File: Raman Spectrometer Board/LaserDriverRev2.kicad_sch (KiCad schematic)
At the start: 40 parts, among them Q5 2N7002, Q6 IRF9Z34, SW1 SW_DPDT_x2, U3 LT1009, U4 OPA4192

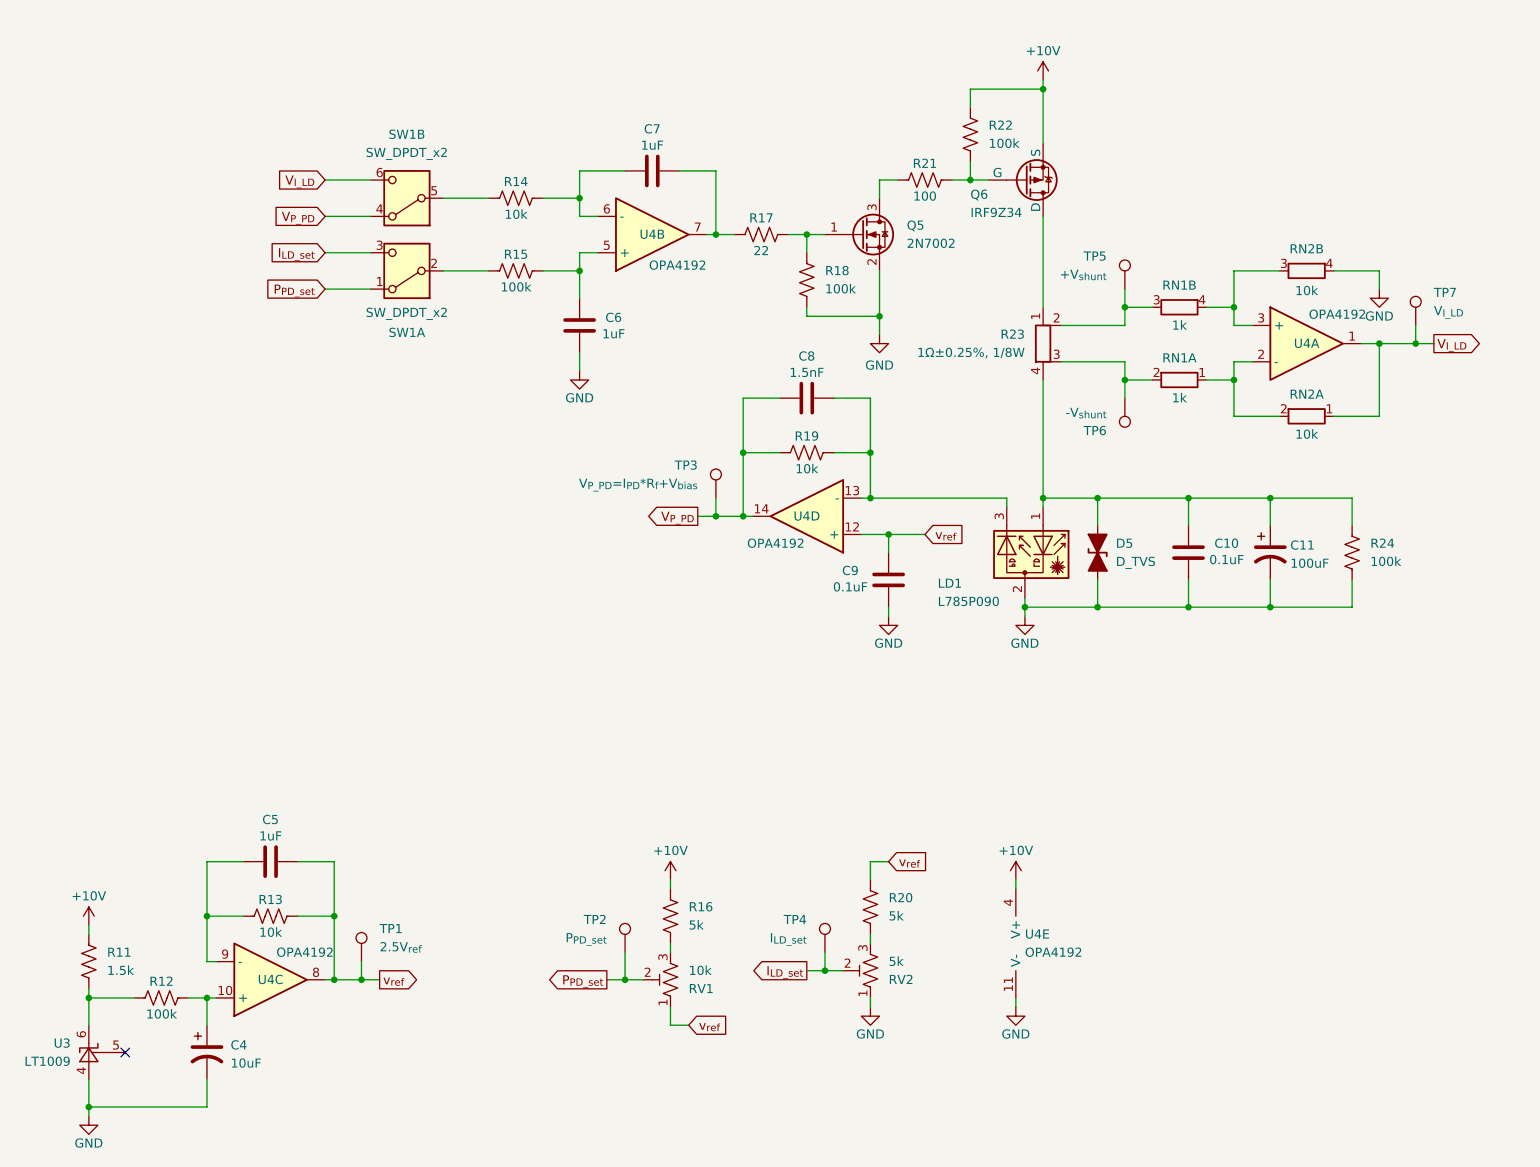
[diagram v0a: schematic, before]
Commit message: Added some laser driver footprints and 3d models
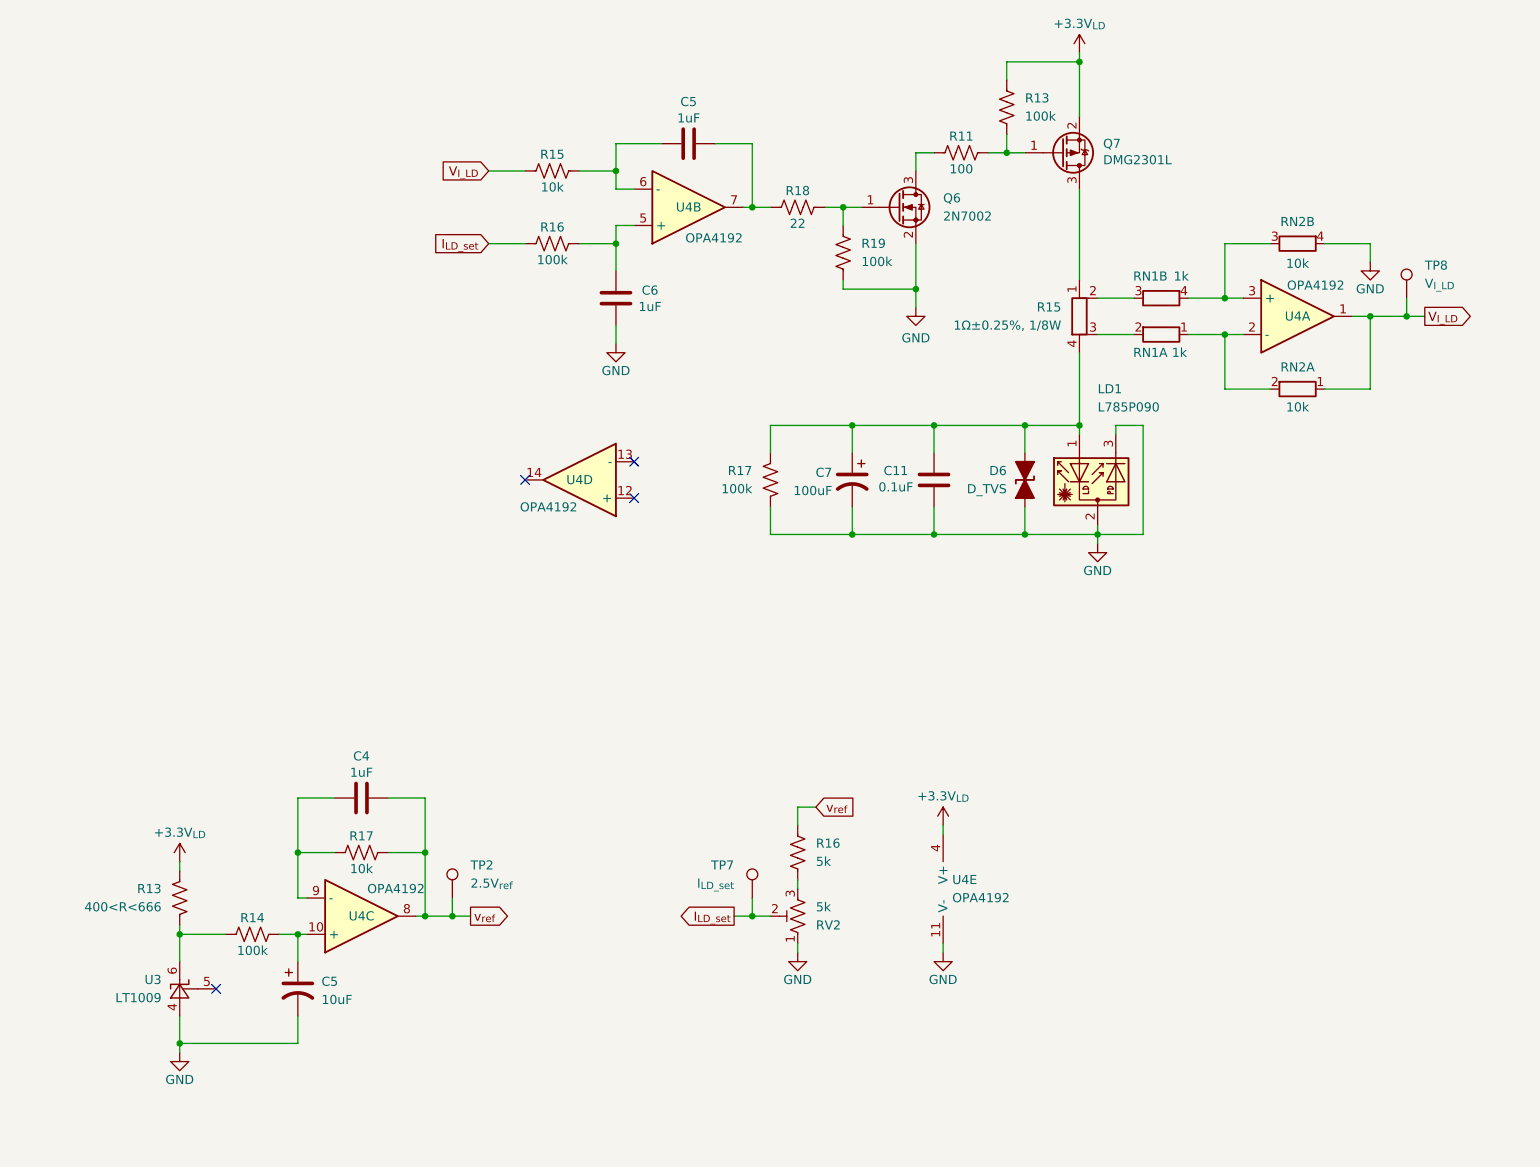
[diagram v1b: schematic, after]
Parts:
- removed C11: 100uF, Capacitor_SMD:CP_Elec_6.3x5.8, symbol Device:C_Polarized_US
- removed C4: 10uF, Capacitor_SMD:CP_Elec_5x5.8, symbol Device:C_Polarized_US
- removed C7: 1uF, Capacitor_SMD:C_0603_1608Metric, symbol Device:C
- removed C8: 1.5nF, Capacitor_SMD:C_0603_1608Metric, symbol Device:C
- removed C9: 0.1uF, Capacitor_SMD:C_0603_1608Metric, symbol Device:C
- removed D5: D_TVS, Diode_SMD:D_0603_1608Metric, symbol Device:D_TVS_Filled
- removed Q5: 2N7002, Package_TO_SOT_SMD:SOT-23, symbol Transistor_FET:2N7002
- removed Q6: IRF9Z34, Package_TO_SOT_THT:TO-220-3_Horizontal_TabUp, symbol Simulation_SPICE:PMOS
- removed R11: 1.5k, Resistor_SMD:R_0603_1608Metric, symbol Device:R_US
- removed R12, R24: 100k, Resistor_SMD:R_0603_1608Metric, symbol Device:R_US
- removed R16, R20: 5k, Resistor_SMD:R_0603_1608Metric, symbol Device:R_US
- removed R17: 22, Resistor_SMD:R_0603_1608Metric, symbol Device:R_US
- removed R23: 1Ω±0.25%, 1/8W, LD_Library:R_Shunt_0805_2012Metric, symbol Device:R_Shunt
- removed RV1: 10k, Potentiometer_THT:Potentiometer_Bourns_3296W_Vertical, symbol Device:R_Potentiometer_Trim_US
- removed SW1: SW_DPDT_x2, Button_Switch_SMD:SW_DPDT_CK_JS202011JCQN, symbol Switch:SW_DPDT_x2
- removed TP2: P_{PD_set}, TestPoint:TestPoint_Pad_D1.5mm, symbol Connector:TestPoint
- removed TP3: V_{P_PD}=I_{PD}*R_{f}+V_{bias}, TestPoint:TestPoint_Pad_D1.5mm, symbol Connector:TestPoint
- removed TP5: +V_{shunt}, TestPoint:TestPoint_Pad_D1.5mm, symbol Connector:TestPoint
- removed TP6: -V_{shunt}, TestPoint:TestPoint_Pad_D1.5mm, symbol Connector:TestPoint
- added C4: 1uF, Capacitor_SMD:C_0603_1608Metric, symbol Device:C
- added C5: 10uF, Capacitor_SMD:CP_Elec_5x5.8, symbol Device:C_Polarized_US
- added C7: 100uF, Capacitor_SMD:CP_Elec_6.3x5.8, symbol Device:C_Polarized_US
- added D6: D_TVS, Diode_SMD:D_0603_1608Metric, symbol Device:D_TVS_Filled
- added Q6: 2N7002, Package_TO_SOT_SMD:SOT-23, symbol Transistor_FET:2N7002
- added Q7: DMG2301L, Package_TO_SOT_SMD:SOT-23, symbol Transistor_FET:DMG2301L
- added R15: 1Ω±0.25%, 1/8W, LD_Library:R_Shunt_0805_2012Metric, symbol Device:R_Shunt
- added R16, R17: 100k, Resistor_SMD:R_0603_1608Metric, symbol Device:R_US
- added R16: 5k, Resistor_SMD:R_0603_1608Metric, symbol Device:R_US
- added R17: 10k, Resistor_SMD:R_0603_1608Metric, symbol Device:R_US
- R13: value 10k -> 400<R<666
- R14: value 10k -> 100k
- R15: value 100k -> 10k
- R18: value 100k -> 22
- R19: value 10k -> 100k; Price $0.23000 -> (none)
- renumbered C10 to C11, R21 to R11, R22 to R13, TP1 to TP2, TP4 to TP7, TP7 to TP8
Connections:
- net GND: now also LD1.3, R19.2, C5.2, C7.2, D6.1 (A1), Q6.2 (S), R17.2; no longer R18.2
- net I_{LD_set}: now also R16.1
- net V_{I_LD}: now also R15.1
- net v_{ref}: now also C4.2, R16.1, R17.2; no longer C5.2, R13.2, U4.12 (+)
- net at U4.10 (+): now also R14.2, C5.1
- net at R11.2, R13.2: now also Q7.1 (G)
- net at R18.1: now also C5.2, U4.7
- net at RN1.2 (R1.2): now also R15.3
- net at C6.2, U4.5 (+): now also R16.2; no longer R15.2
- net at U4.6 (-): now also C5.1, R15.2; no longer R14.2
- net at RV2.3: now also R16.2
- net at RN1.3 (R2.1): now also R15.2
- net at C11.1, LD1.1: now also C7.1, D6.2 (A2), R15.4, R17.1
- net at U3.6 (K), U3.8 (K): now also R13.2, R14.1
- net at R11.1: now also Q6.3 (D)
- net +10V renamed +3.3V_{LD}
- net +3.3V_{LD}: now also R13.1, Q7.2 (S)
- net V_{P_PD}: no longer names the net of R19.1
- net V_{P_PD}: now also R18.2, Q6.1 (G); no longer U4.14
- new net: C4.1, R17.1, U4.9 (-)
- new net: Q7.3 (D), R15.1
- now unconnected: U4.13 (-)
- no-connect marks 1 -> 4
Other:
- moved on the sheet: C11, LD1, R11, R13, RN1A, RN1B, RN2A, RN2B, RV2, TP2, TP7, TP8

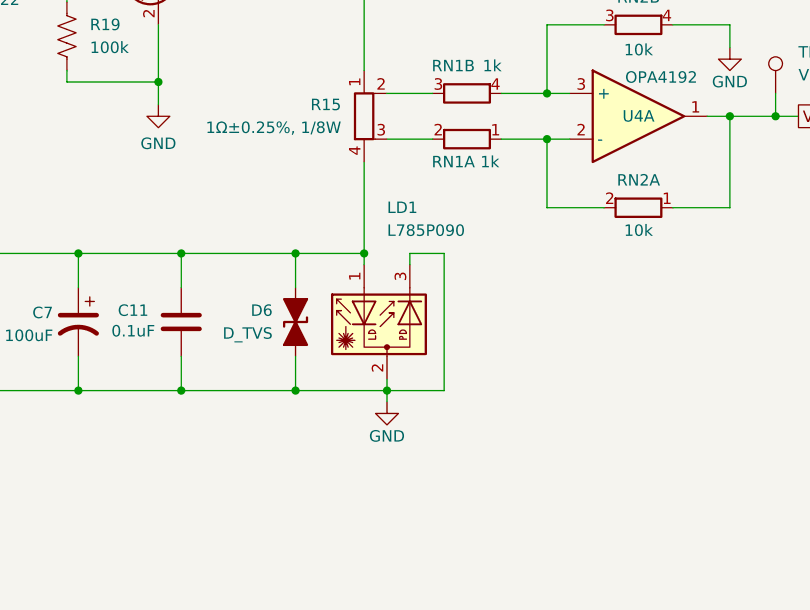
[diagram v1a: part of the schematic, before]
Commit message: Validated all footprints and models
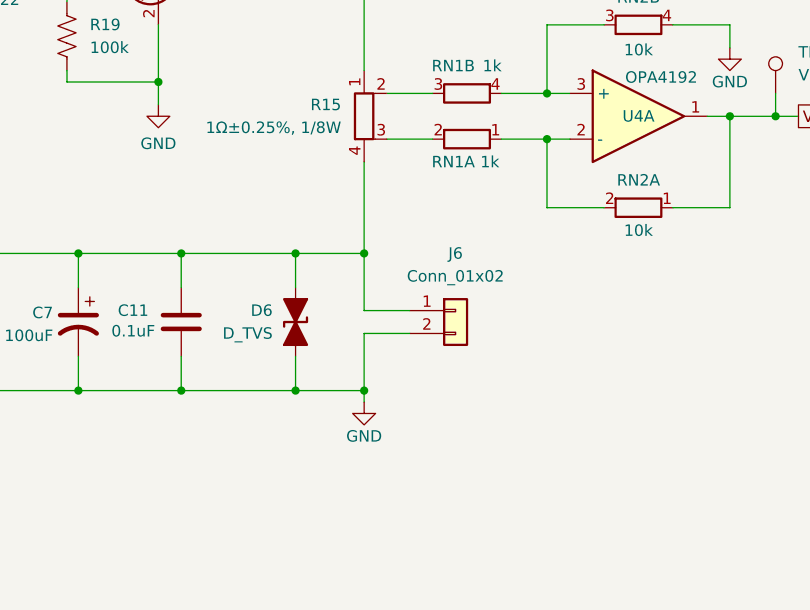
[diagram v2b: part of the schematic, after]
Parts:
- removed LD1: L785P090, LD_Library:S7060R - Laser Diode Socket for Ø5.6 mm Laser, 3 Pin, symbol Device:D_Laser_Photo_PType
- added J6: Conn_01x02, Connector_JST:JST_EH_S2B-EH_1x02_P2.50mm_Horizontal, symbol Connector_Generic:Conn_01x02
- R15: footprint LD_Library:R_Shunt_0805_2012Metric -> LaserDriverRev2Library:R_Shunt_0805_2012Metric
- RN1, RN2: footprint Resistor_SMD:R_Array_Convex_2x0606 -> LaserDriverRev2Library:R_Array_Convex_2x0606
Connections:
- net GND: now also J6.2 (Pin_2)
- net at C11.1, C7.1, D6.2 (A2)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: now also J6.1 (Pin_1)

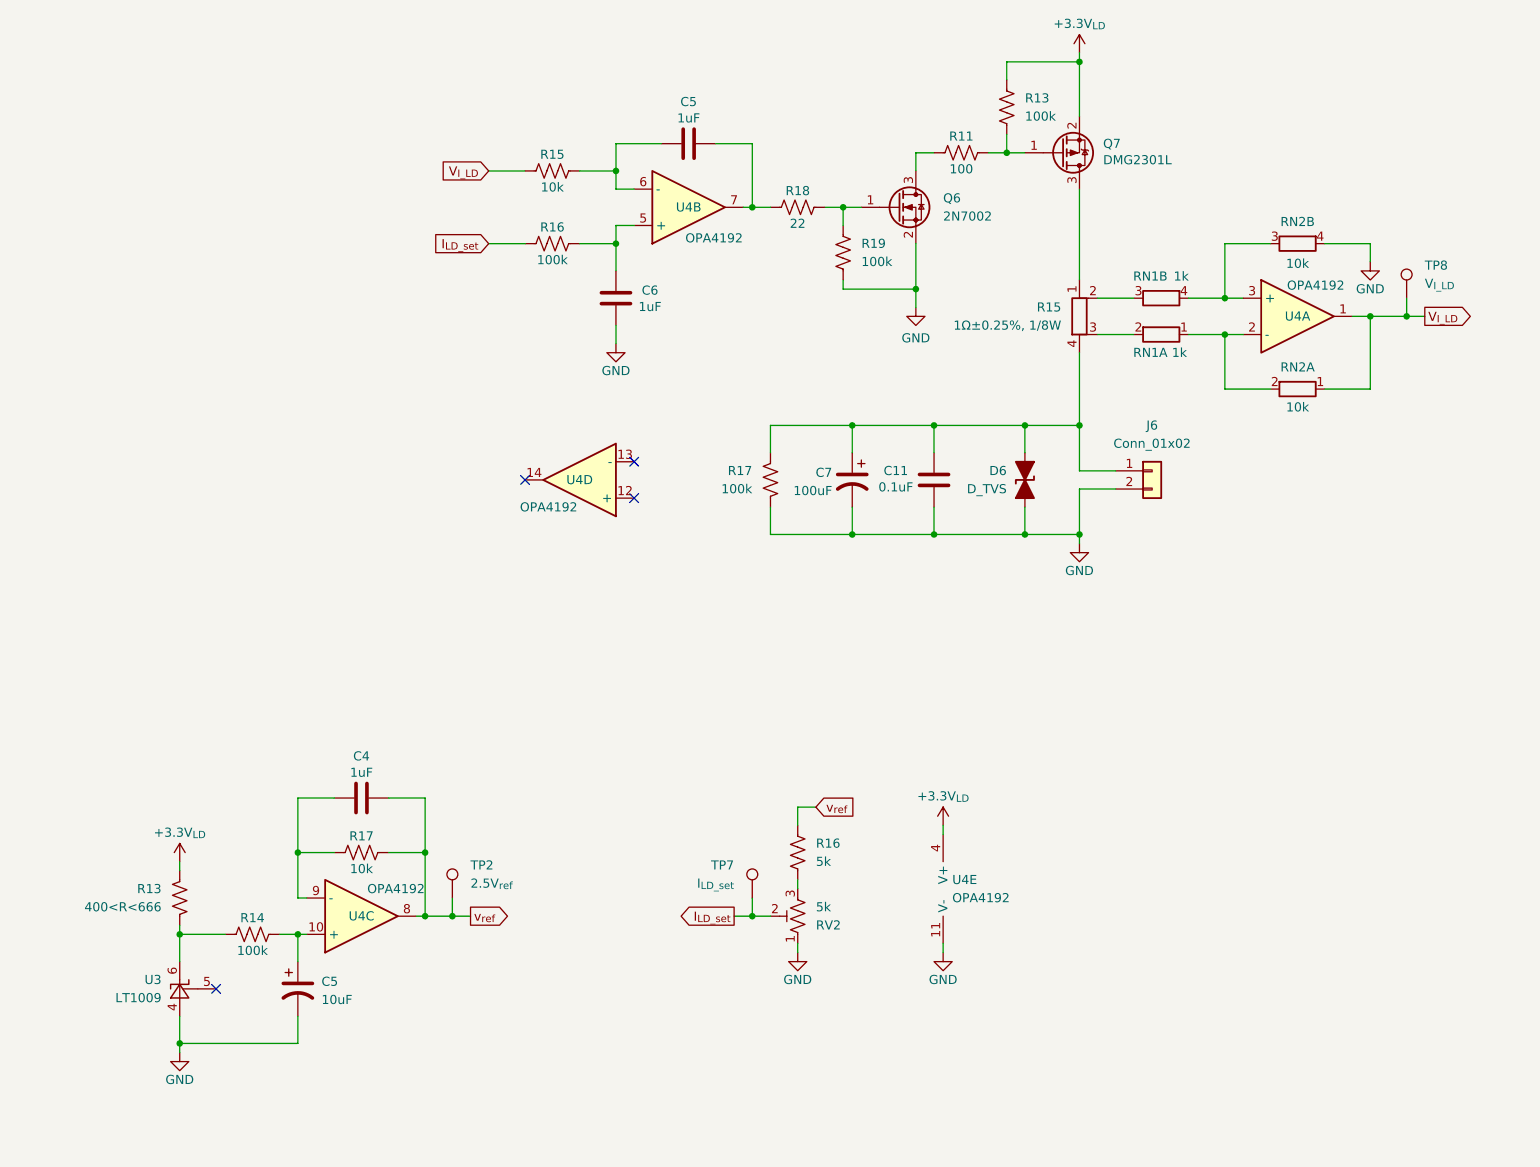
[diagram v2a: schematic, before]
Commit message: Began re-laying out laser driver section
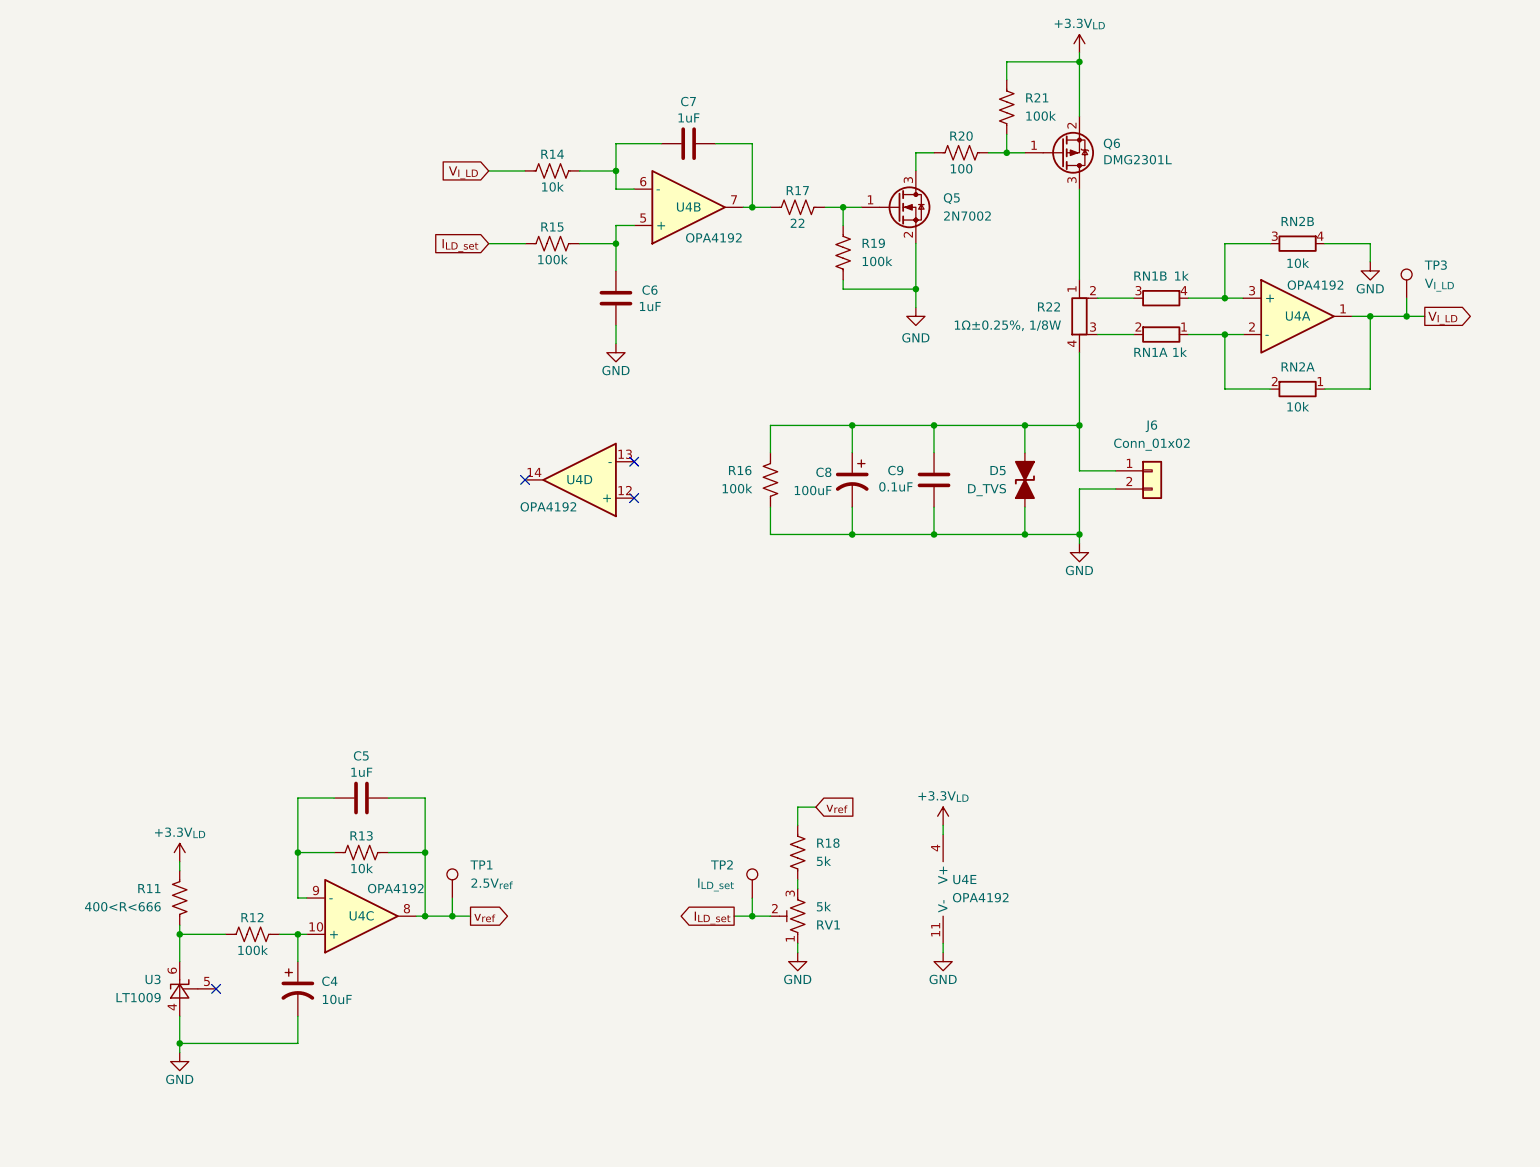
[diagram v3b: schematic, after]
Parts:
- renumbered C5 to C4, C4 to C5, C5 to C7, C7 to C8, C11 to C9, D6 to D5, Q6 to Q5, Q7 to Q6, R13 to R11, R14 to R12, R17 to R13, R15 to R14, R16 to R15, R17 to R16, R18 to R17, R16 to R18, R11 to R20, R13 to R21, R15 to R22, RV2 to RV1, TP2 to TP1, TP7 to TP2, TP8 to TP3
